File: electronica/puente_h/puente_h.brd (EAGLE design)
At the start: 70.8 x 118.7 mm, 40 parts, among them IC1 7805, IC2 7812, IC3 7404LP, IC4 7408LP, IC5 ADUM1400, Q1 IRF2804, Q2 IRF2804, Q5 IRF2804, Q6 IRF2804, U1 IR2110LP

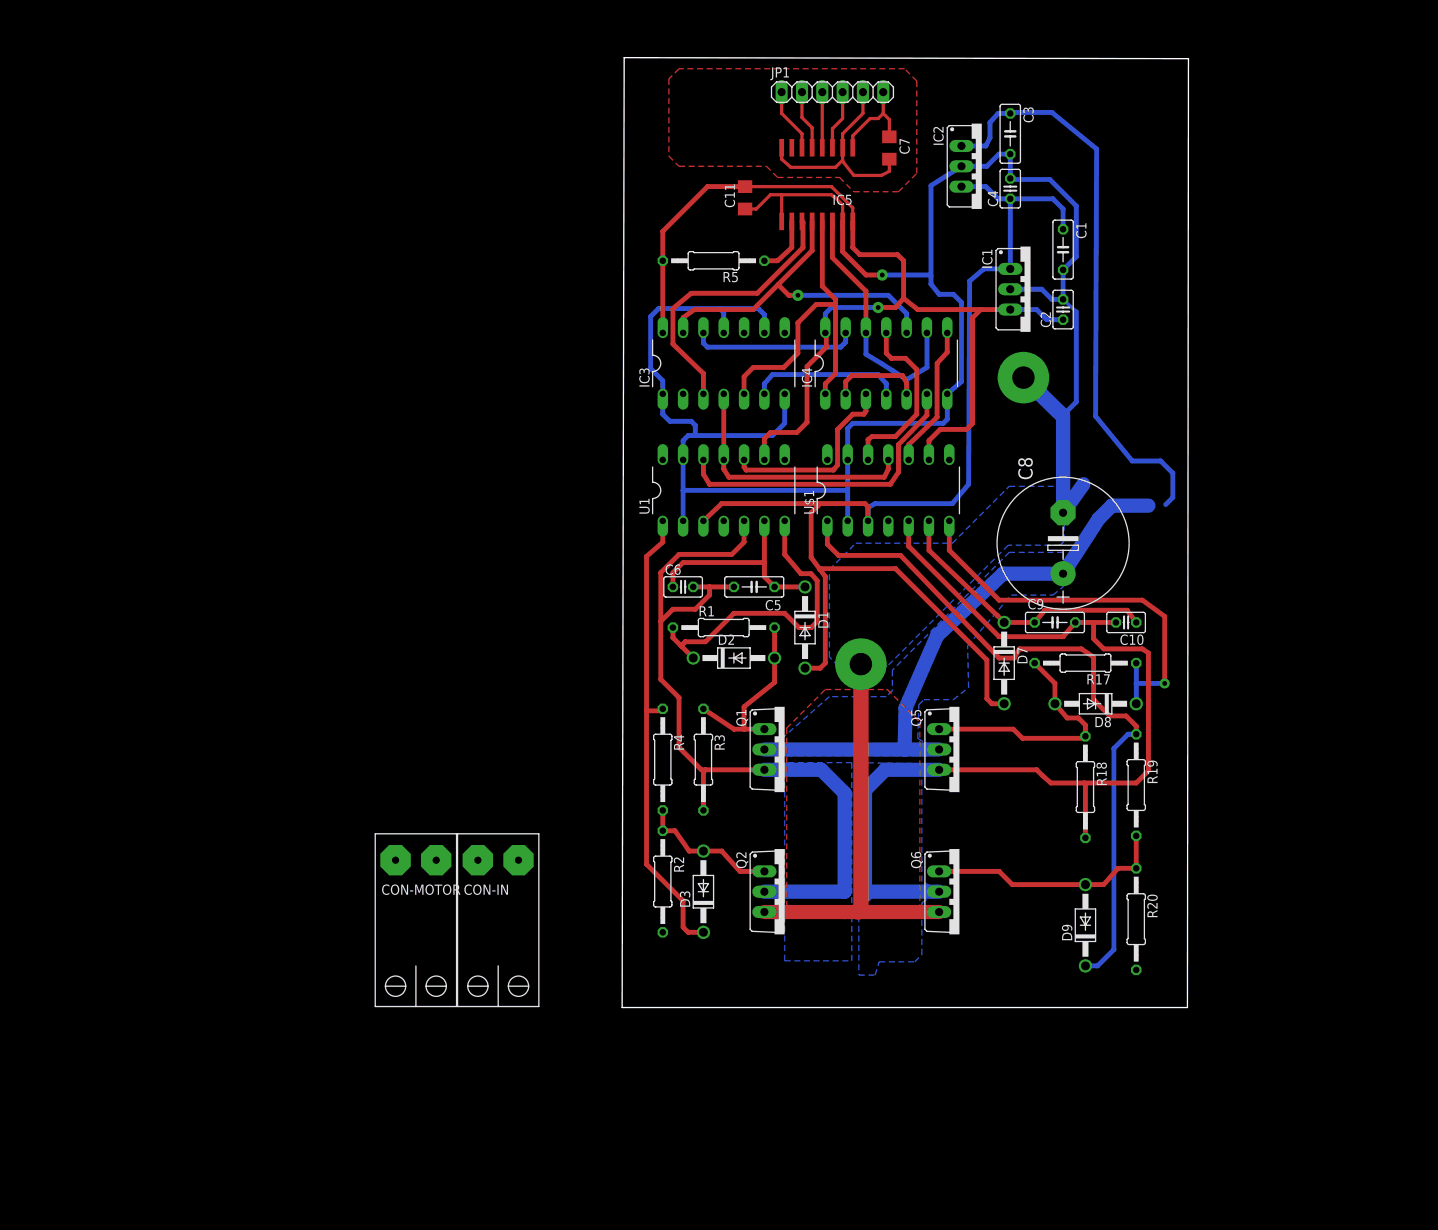
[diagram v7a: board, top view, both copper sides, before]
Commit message: conectores puente h
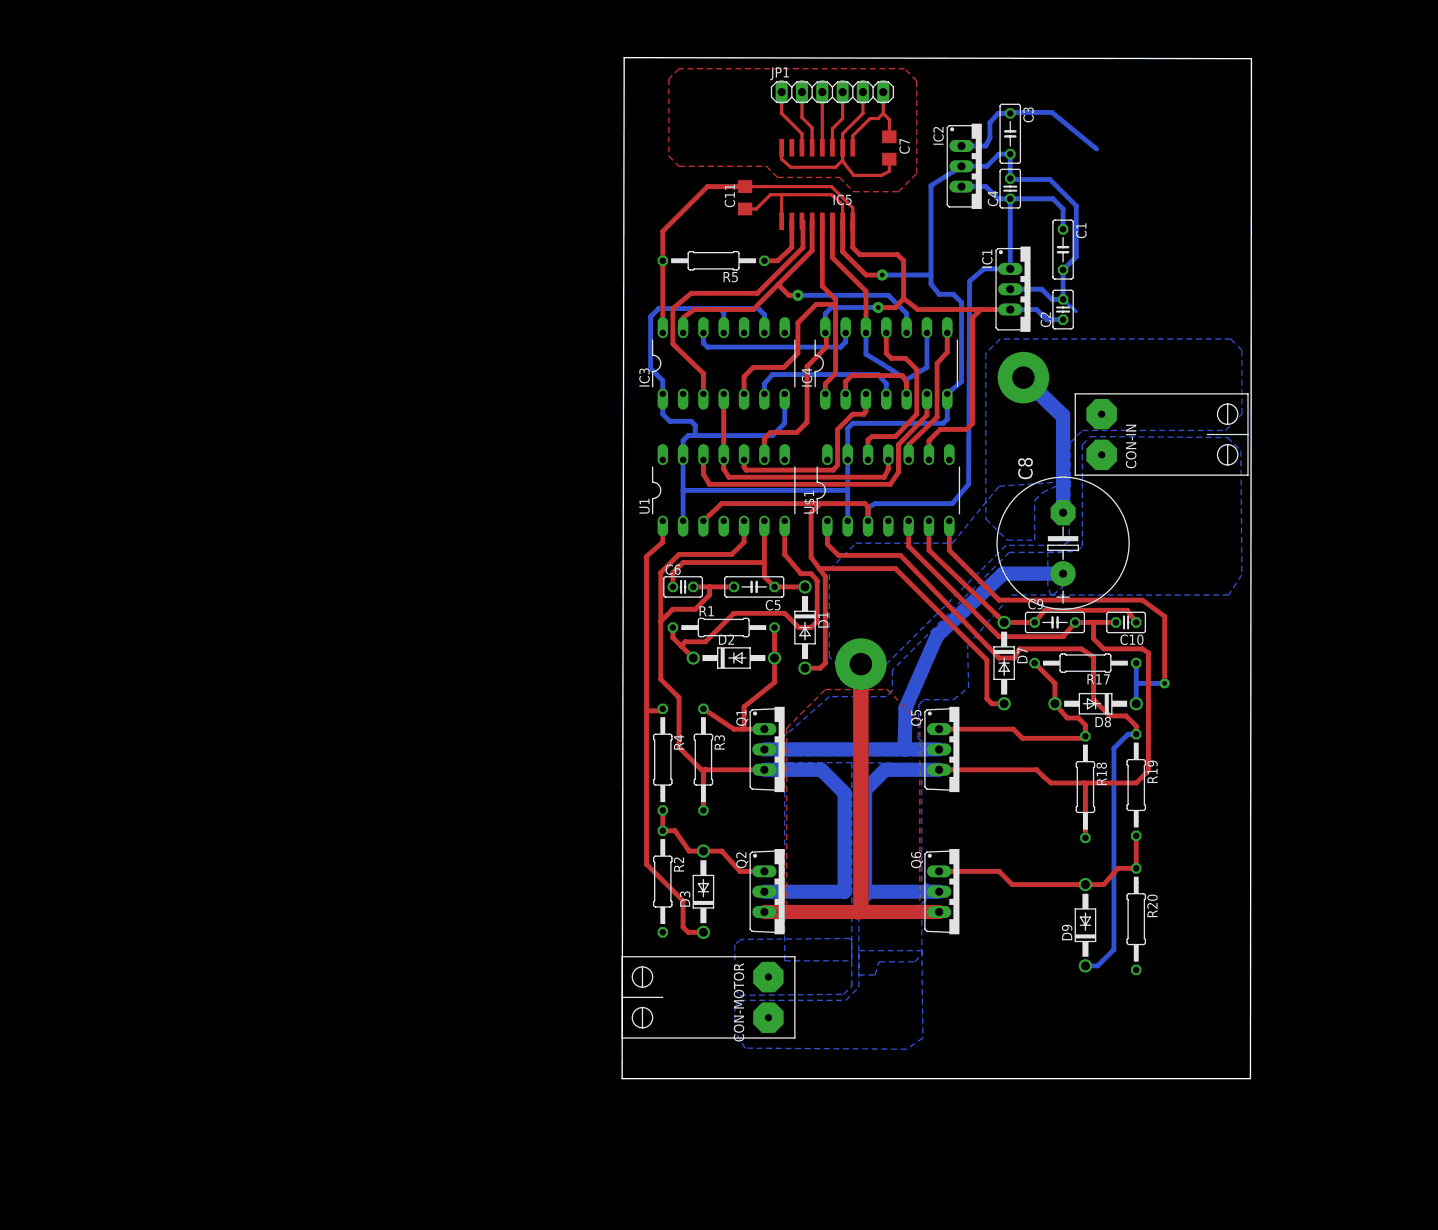
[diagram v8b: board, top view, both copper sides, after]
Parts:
- moved CON-IN 94.8 mm to (61.7, 74.9), turned to 90 degrees
- moved CON-MOTOR 45.0 mm to (16.5, 4.57), turned to 270 degrees
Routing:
- net VIN: track 143.0 -> 77.3 mm
- net GND: track 316.8 -> 298.8 mm
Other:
- board size 70.8 x 118.7 mm -> 78.7 x 127.6 mm
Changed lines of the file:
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@@
 <board>
 <plain>
-<wire x1="0" y1="3.302" x2="70.663" y2="3.302" width="0" layer="20"/>
-<wire x1="70.663" y1="3.302" x2="70.79" y2="121.91" width="0" layer="20"/>
-<wire x1="70.79" y1="121.91" x2="0.254" y2="122.037" width="0" layer="20"/>
-<wire x1="0.254" y1="122.037" x2="0" y2="3.302" width="0" layer="20"/>
+<wire x1="0" y1="-5.588" x2="78.537" y2="-5.588" width="0" layer="20"/>
+<wire x1="78.537" y1="-5.588" x2="78.664" y2="121.91" width="0" layer="20"/>
+<wire x1="78.664" y1="121.91" x2="0.254" y2="122.037" width="0" layer="20"/>
+<wire x1="0.254" y1="122.037" x2="0" y2="-5.588" width="0" layer="20"/>
 </plain>
 <attributes>
@@
 <element name="U1" library="components" package="IR2110-LP" value="IR2110LP" x="11.43" y="67.945"/>
 <element name="U$1" library="components" package="IR2110-LP" value="IR2110LP" x="32.004" y="67.945"/>
-<element name="CON-IN" library="components" package="METALTEX-2" value="METALTEX-2" x="-15.494" y="19.939"/>
-<element name="CON-MOTOR" library="components" package="METALTEX-2" value="METALTEX-2" x="-25.781" y="19.939"/>
+<element name="CON-IN" library="components" package="METALTEX-2" value="METALTEX-2" x="61.722" y="74.93" rot="R90"/>
+<element name="CON-MOTOR" library="components" package="METALTEX-2" value="METALTEX-2" x="16.51" y="4.572" rot="R270"/>
 </elements>
 <signals>
@@
 <wire x1="29.845" y1="15.621" x2="29.464" y2="15.24" width="1.9304" layer="1"/>
 <wire x1="54.991" y1="77.343" x2="50.165" y2="82.042" width="1.9304" layer="16"/>
-<wire x1="56.769" y1="90.297" x2="56.769" y2="78.994" width="0.6096" layer="16"/>
-<wire x1="56.769" y1="78.994" x2="55.118" y2="77.343" width="0.6096" layer="16"/>
 <wire x1="55.118" y1="77.343" x2="54.61" y2="78.105" width="0.6096" layer="16"/>
 <wire x1="54.61" y1="78.105" x2="54.991" y2="77.343" width="0.6096" layer="16"/>
@@
 </polygon>
 <contactref element="C8" pad="-"/>
-<wire x1="57.658" y1="68.707" x2="55.118" y2="65.151" width="1.778" layer="16"/>
 <wire x1="55.118" y1="65.151" x2="55.118" y2="77.343" width="1.778" layer="16"/>
 <contactref element="IC3" pad="11"/>
@@
 <wire x1="17.018" y1="90.678" x2="12.192" y2="90.678" width="0.6096" layer="16"/>
 <polygon width="0.4064" layer="16" rank="2">
-<vertex x="55.245" y="68.453"/>
-<vertex x="55.245" y="61.595"/>
-<vertex x="54.737" y="61.087"/>
-<vertex x="48.26" y="61.087"/>
-<vertex x="33.147" y="45.974"/>
+<vertex x="56.007" y="69.088"/>
+<vertex x="55.88" y="61.595"/>
+<vertex x="55.118" y="61.087"/>
+<vertex x="48.006" y="61.087"/>
+<vertex x="32.766" y="45.974"/>
 <vertex x="27.051" y="45.974"/>
 <vertex x="25.908" y="47.117"/>
@@
 <vertex x="29.21" y="61.341"/>
 <vertex x="41.275" y="61.341"/>
-<vertex x="48.387" y="68.453"/>
+<vertex x="47.117" y="68.453"/>
 </polygon>
 <contactref element="CON-IN" pad="P2"/>
+<polygon width="0.4064" layer="16" isolate="0.3048">
+<vertex x="56.007" y="68.326"/>
+<vertex x="56.007" y="73.914"/>
+<vertex x="57.531" y="75.438"/>
+<vertex x="75.438" y="75.438"/>
+<vertex x="77.47" y="77.47"/>
+<vertex x="77.47" y="85.471"/>
+<vertex x="76.073" y="86.868"/>
+<vertex x="47.244" y="86.868"/>
+<vertex x="45.466" y="85.09"/>
+<vertex x="45.466" y="64.389"/>
+<vertex x="48.133" y="61.722"/>
+<vertex x="51.562" y="61.722"/>
+<vertex x="51.562" y="66.675"/>
+<vertex x="52.578" y="67.691"/>
+<vertex x="55.372" y="68.961"/>
+</polygon>
 <wire x1="39.624" y1="15.24" x2="64.262" y2="8.001" width="0" layer="19" extent="1-1"/>
+<wire x1="42.418" y1="81.534" x2="50.165" y2="82.042" width="0" layer="19" extent="16-16"/>
 <wire x1="5.08" y1="12.7" x2="17.78" y2="15.24" width="0" layer="19" extent="1-1"/>
-<wire x1="-12.954" y1="21.717" x2="5.08" y2="12.7" width="0" layer="19" extent="1-1"/>
 </signal>
 <signal name="VIN">
@@
 <wire x1="45.974" y1="113.919" x2="46.99" y2="115.062" width="0.6096" layer="16"/>
 <wire x1="46.99" y1="115.062" x2="48.514" y2="115.062" width="0.6096" layer="16"/>
-<wire x1="67.945" y1="66.167" x2="68.834" y2="67.056" width="0.6096" layer="16"/>
-<wire x1="68.834" y1="67.056" x2="68.834" y2="70.104" width="0.6096" layer="16"/>
-<wire x1="68.834" y1="70.104" x2="67.31" y2="71.628" width="0.6096" layer="16"/>
-<wire x1="67.31" y1="71.628" x2="63.754" y2="71.628" width="0.6096" layer="16"/>
-<wire x1="63.754" y1="71.628" x2="59.182" y2="77.216" width="0.6096" layer="16"/>
-<wire x1="59.182" y1="77.216" x2="59.309" y2="110.617" width="0.6096" layer="16"/>
 <wire x1="59.309" y1="110.617" x2="53.721" y2="115.189" width="0.6096" layer="16"/>
 <wire x1="53.721" y1="115.189" x2="48.641" y2="115.189" width="0.6096" layer="16"/>
 <wire x1="48.641" y1="115.189" x2="48.514" y2="115.062" width="0.6096" layer="16"/>
-<wire x1="55.118" y1="57.531" x2="59.563" y2="64.389" width="1.778" layer="16"/>
-<wire x1="59.563" y1="64.389" x2="61.214" y2="66.04" width="1.778" layer="16"/>
-<wire x1="61.214" y1="66.04" x2="65.786" y2="66.04" width="1.778" layer="16"/>
 <wire x1="17.78" y1="35.56" x2="35.306" y2="35.56" width="1.778" layer="16"/>
 <wire x1="35.306" y1="35.56" x2="39.624" y2="35.56" width="1.778" layer="16"/>
@@
 </polygon>
 <contactref element="CON-IN" pad="P1"/>
-<wire x1="65.786" y1="66.04" x2="67.945" y2="66.167" width="0" layer="19" extent="16-16"/>
-<wire x1="-18.034" y1="21.717" x2="17.78" y2="35.56" width="0" layer="19" extent="1-1"/>
+<polygon width="0.4064" layer="16" isolate="0.6096">
+<vertex x="58.547" y="74.676"/>
+<vertex x="75.692" y="74.549"/>
+<vertex x="77.343" y="72.898"/>
+<vertex x="77.47" y="57.404"/>
+<vertex x="75.819" y="54.864"/>
+<vertex x="53.594" y="54.864"/>
+<vertex x="53.213" y="56.007"/>
+<vertex x="53.213" y="60.198"/>
+<vertex x="56.896" y="60.325"/>
+<vertex x="57.531" y="60.96"/>
+<vertex x="57.531" y="73.66"/>
+</polygon>
+<wire x1="59.944" y1="72.39" x2="59.309" y2="110.617" width="0" layer="19" extent="16-16"/>
 </signal>
 <signal name="+5V">
@@
 </polygon>
 <contactref element="CON-MOTOR" pad="P1"/>
-<wire x1="7.112" y1="35.814" x2="-28.321" y2="21.717" width="0" layer="19" extent="1-1"/>
+<polygon width="0.4064" layer="16" isolate="0.4064" rank="2">
+<vertex x="14.097" y="5.588"/>
+<vertex x="14.732" y="4.826"/>
+<vertex x="27.686" y="4.953"/>
+<vertex x="28.702" y="5.969"/>
+<vertex x="28.702" y="11.684"/>
+<vertex x="28.448" y="11.938"/>
+<vertex x="14.859" y="11.811"/>
+<vertex x="14.097" y="11.176"/>
+</polygon>
 </signal>
 <signal name="N$2">
@@
 <wire x1="51.816" y1="33.02" x2="39.624" y2="33.02" width="0.6096" layer="1"/>
 <contactref element="CON-MOTOR" pad="P2"/>
-<wire x1="30.353" y1="17.272" x2="-23.241" y2="21.717" width="0" layer="19" extent="16-16"/>
+<polygon width="0.4064" layer="16">
+<vertex x="14.732" y="4.191"/>
+<vertex x="27.94" y="4.191"/>
+<vertex x="29.591" y="5.842"/>
+<vertex x="29.591" y="10.414"/>
+<vertex x="37.465" y="10.414"/>
+<vertex x="37.592" y="-0.508"/>
+<vertex x="35.56" y="-1.905"/>
+<vertex x="15.367" y="-1.778"/>
+<vertex x="14.097" y="0.381"/>
+<vertex x="14.097" y="3.429"/>
+</polygon>
 </signal>
 <signal name="N$32">
